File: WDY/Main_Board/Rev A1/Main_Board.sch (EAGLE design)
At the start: 188 parts, among them J1 22-05-7028-02, J10 22-05-7038-03, J11 22-05-7028-02, J12 22-05-7028-02, J13 22-05-7028-02, J14 22-05-7028-02, J15 22-05-7058-05, J2 22-05-7028-02, J3 22-05-7048-04, J4 22-05-7048-04, J5 1241050-5, J6 90814-0208, J7 90814-0206, J8 90814-0208, J9 22-05-7038-03, K1 G6K-2G-Y, K2 G6K-2G-Y, K3 G6K-2G-Y, K4 G6K-2G-Y, P1 RB1-125BAG1A, SW1 B3FS-1015, SW2 B3FS-1015, T1 MMBT2222AL, U1 LPC1768FBD100, U11 SN74LVC3G17DCTR, U2 SN74LVC3G17DCTR, U3 SN74LVC3G17DCTR, U4 TPL0401A, U5 AT24C512C-SSHM-B, U6 SN74LVC2G17DBVR, U7 SN74LVC2G17DBVR, U8 LT1767EMS8E-5PBF, U9 TC1264-3.3, X1 FC-135, X2 MSTBA2

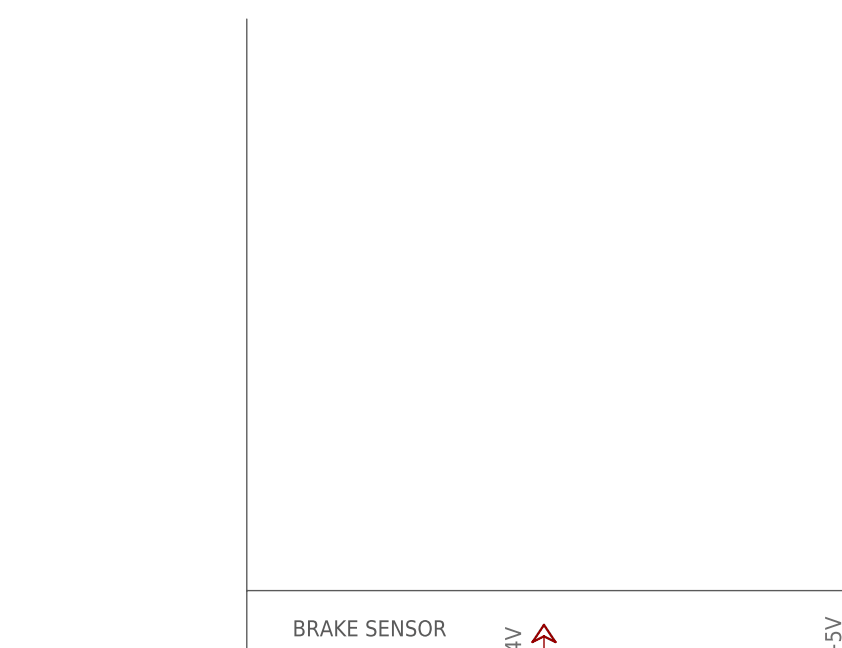
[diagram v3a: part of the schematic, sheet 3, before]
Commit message: Finishing routing and adding FTDI connector
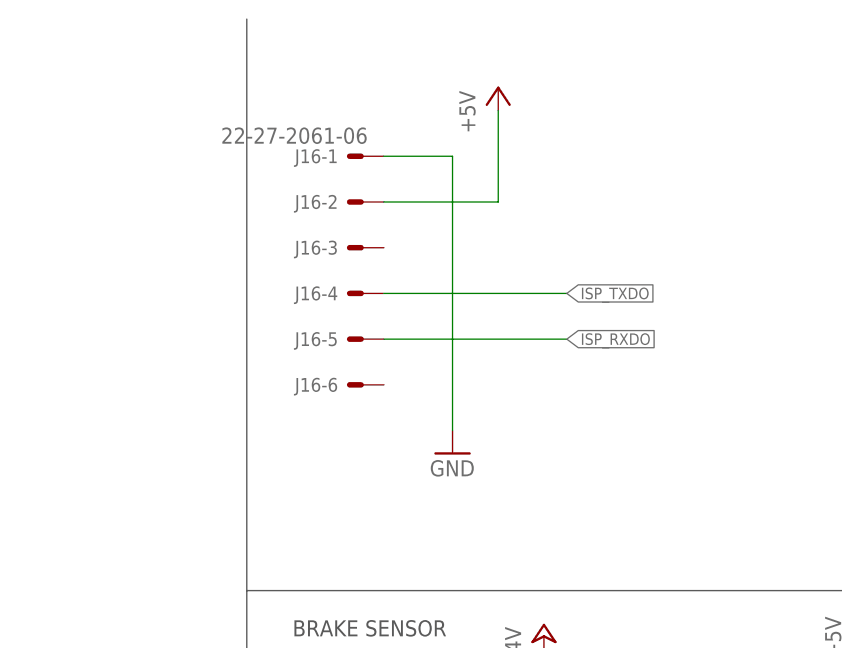
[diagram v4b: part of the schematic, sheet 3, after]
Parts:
- added J16: 22-27-2061-06, con-molex:22-27-2061-06
- added TP3: TPB1,27, testpad:TPB1,27
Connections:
- net +5V: now also J16-2.S
- net EEPROM_SCL: now also U1.P0[28]/SCL0/USB_SCL
- net EEPROM_SDA: now also U1.P0[27]/SDA0/USB_SDA
- net GND: now also J16-1.S, TP3.TP
- net HMI_LCD_BACKLIGHT: now also U1.P0[22]/RTS1/TD1
- net ISP_RXDO: now also J16-5.S
- net ISP_TXDO: now also J16-4.S
- net VBAT+: now also U1.VBAT
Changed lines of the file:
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@@
 <class number="1" name="signal" width="0.1778" drill="0.35">
 </class>
-<class number="2" name="supply" width="0.4064" drill="0.5">
+<class number="2" name="supply" width="0.007740625" drill="0.5">
 </class>
 </classes>
@@
 <part name="GND89" library="supply1" deviceset="GND" device=""/>
 <part name="R70" library="rcl" deviceset="R-EU_" device="R0603" value="100"/>
+<part name="J16" library="con-molex" deviceset="22-?-06" device="27-2061"/>
+<part name="P+23" library="supply1" deviceset="+5V" device=""/>
+<part name="GND90" library="supply1" deviceset="GND" device=""/>
+<part name="TP3" library="testpad" deviceset="TP" device="B1,27"/>
 </parts>
 <sheets>
@@
 </segment>
 <segment>
-<wire x1="132.08" y1="172.72" x2="124.46" y2="172.72" width="0.1524" layer="91"/>
 <label x="124.46" y="172.72" size="1.27" layer="95" rot="R180" xref="yes"/>
+<pinref part="U1" gate="A" pin="P0[27]/SDA0/USB_SDA"/>
+<wire x1="124.46" y1="172.72" x2="132.08" y2="172.72" width="0.1524" layer="91"/>
 </segment>
 </net>
@@
 </segment>
 <segment>
-<wire x1="132.08" y1="175.26" x2="124.46" y2="175.26" width="0.1524" layer="91"/>
 <label x="124.46" y="175.26" size="1.27" layer="95" rot="R180" xref="yes"/>
+<pinref part="U1" gate="A" pin="P0[28]/SCL0/USB_SCL"/>
+<wire x1="124.46" y1="175.26" x2="132.08" y2="175.26" width="0.1524" layer="91"/>
 </segment>
 </net>
@@
 </segment>
 <segment>
-<wire x1="134.62" y1="187.96" x2="124.46" y2="187.96" width="0.1524" layer="91"/>
 <label x="124.46" y="187.96" size="1.27" layer="95" rot="R180" xref="yes"/>
+<pinref part="U1" gate="A" pin="VBAT"/>
+<wire x1="124.46" y1="187.96" x2="132.08" y2="187.96" width="0.1524" layer="91"/>
+</segment>
+</net>
+<net name="HMI_LCD_BACKLIGHT" class="0">
+<segment>
+<wire x1="314.96" y1="121.92" x2="320.04" y2="121.92" width="0.1524" layer="91"/>
+<label x="320.04" y="121.92" size="1.27" layer="95" xref="yes"/>
+<pinref part="U1" gate="A" pin="P0[22]/RTS1/TD1"/>
 </segment>
 </net>
@@
 <instance part="U$12" gate="A" x="40.64" y="248.92"/>
 <instance part="U$13" gate="A" x="320.04" y="167.64"/>
+<instance part="J16" gate="-1" x="134.62" y="241.3" rot="MR0"/>
+<instance part="J16" gate="-2" x="134.62" y="236.22" rot="MR0"/>
+<instance part="J16" gate="-3" x="134.62" y="231.14" rot="MR0"/>
+<instance part="J16" gate="-4" x="134.62" y="226.06" rot="MR0"/>
+<instance part="J16" gate="-5" x="134.62" y="220.98" rot="MR0"/>
+<instance part="J16" gate="-6" x="134.62" y="215.9" rot="MR0"/>
+<instance part="P+23" gate="1" x="149.86" y="248.92"/>
+<instance part="GND90" gate="1" x="144.78" y="208.28"/>
 </instances>
 <busses>
@@
 <wire x1="320.04" y1="137.16" x2="320.04" y2="134.62" width="0.1524" layer="91"/>
 </segment>
+<segment>
+<pinref part="J16" gate="-1" pin="S"/>
+<pinref part="GND90" gate="1" pin="GND"/>
+<wire x1="137.16" y1="241.3" x2="144.78" y2="241.3" width="0.1524" layer="91"/>
+<wire x1="144.78" y1="241.3" x2="144.78" y2="210.82" width="0.1524" layer="91"/>
+</segment>
 </net>
 <net name="+3V3" class="2">
@@
 <junction x="25.4" y="86.36"/>
 </segment>
+<segment>
+<pinref part="J16" gate="-2" pin="S"/>
+<wire x1="137.16" y1="236.22" x2="149.86" y2="236.22" width="0.1524" layer="91"/>
+<wire x1="149.86" y1="236.22" x2="149.86" y2="246.38" width="0.1524" layer="91"/>
+<pinref part="P+23" gate="1" pin="+5V"/>
+</segment>
 </net>
 <net name="N$21" class="0">
@@
 </segment>
 </net>
+<net name="ISP_TXDO" class="1">
+<segment>
+<pinref part="J16" gate="-4" pin="S"/>
+<wire x1="137.16" y1="226.06" x2="157.48" y2="226.06" width="0.1524" layer="91"/>
+<label x="157.48" y="226.06" size="1.27" layer="95" xref="yes"/>
+</segment>
+</net>
+<net name="ISP_RXDO" class="1">
+<segment>
+<pinref part="J16" gate="-5" pin="S"/>
+<wire x1="137.16" y1="220.98" x2="157.48" y2="220.98" width="0.1524" layer="91"/>
+<label x="157.48" y="220.98" size="1.27" layer="95" xref="yes"/>
+</segment>
+</net>
 </nets>
 </sheet>
@@
 <instance part="MP3" gate="1" x="327.66" y="236.22"/>
 <instance part="MP4" gate="1" x="355.6" y="236.22"/>
+<instance part="TP3" gate="G$1" x="106.68" y="195.58" rot="R180"/>
 </instances>
 <busses>
@@
 <wire x1="106.68" y1="200.66" x2="88.9" y2="200.66" width="0.1524" layer="91"/>
 <junction x="88.9" y="200.66"/>
+<pinref part="TP3" gate="G$1" pin="TP"/>
+<wire x1="106.68" y1="198.12" x2="106.68" y2="200.66" width="0.1524" layer="91"/>
+<junction x="106.68" y="200.66"/>
 </segment>
 <segment>

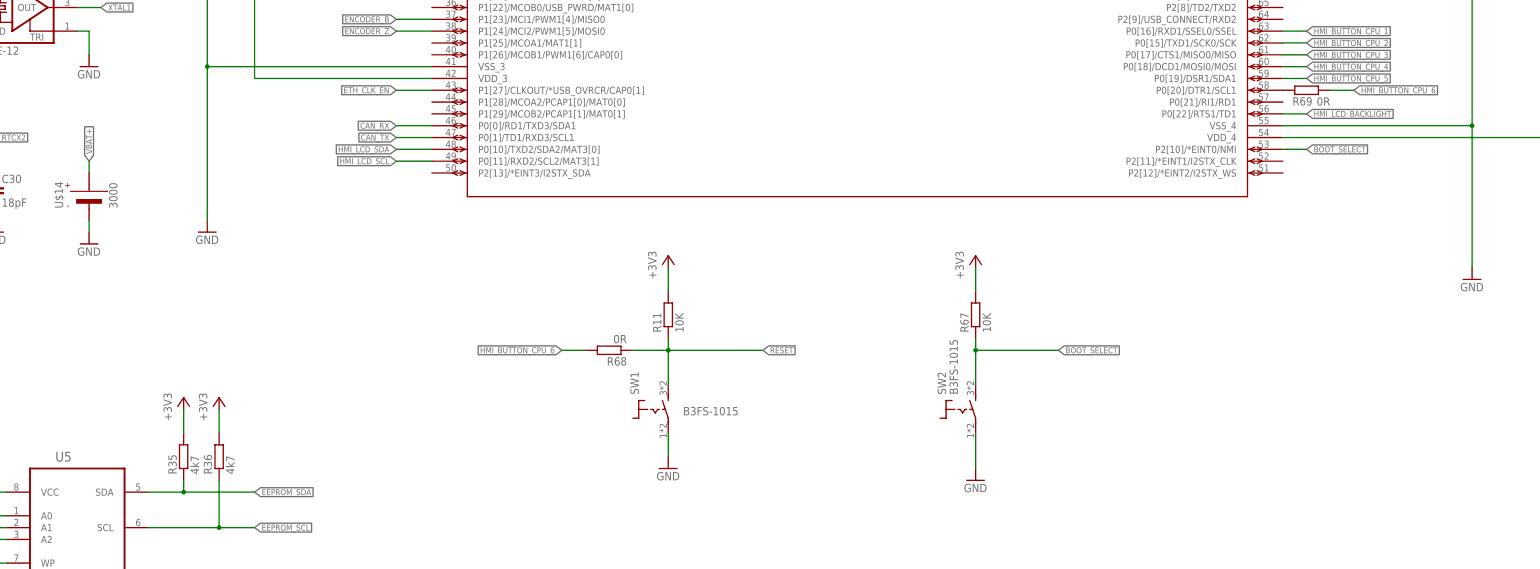
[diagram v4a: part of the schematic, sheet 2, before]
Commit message: Fix :  HMI_BUTTON_CPU_6 configuration is misleading
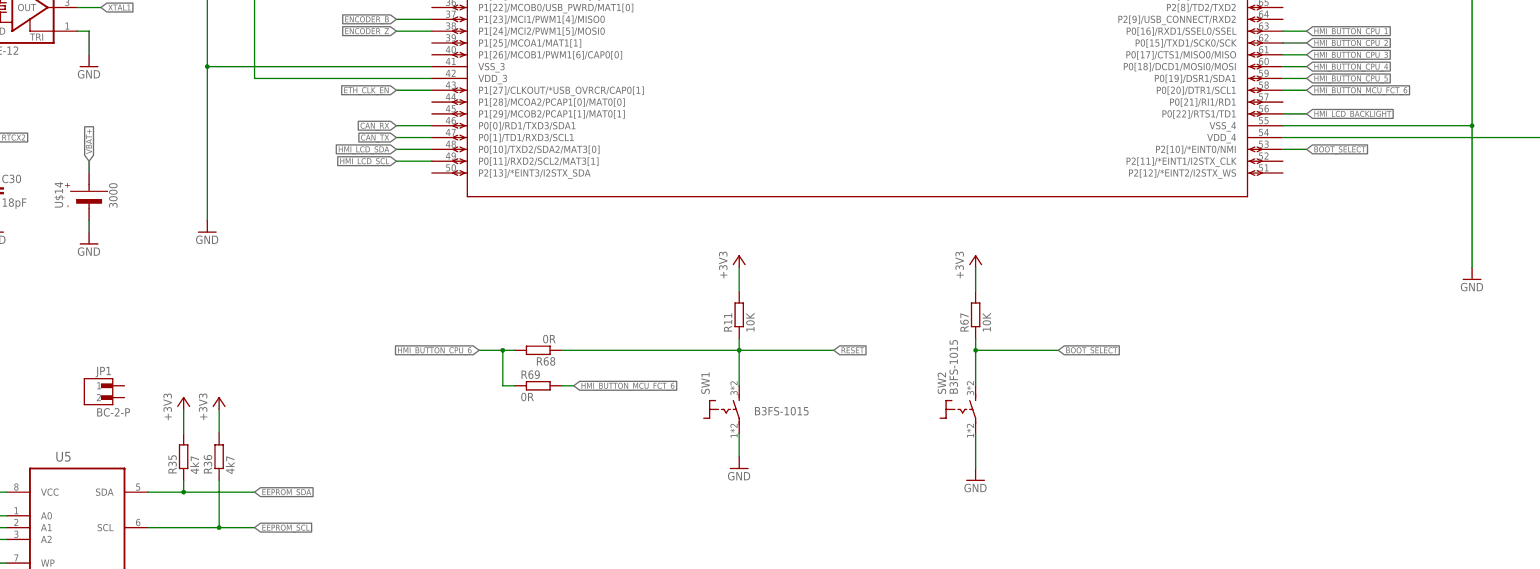
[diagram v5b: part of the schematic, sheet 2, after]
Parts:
- added JP1: BC-2-P, exmachina:BC-2-P
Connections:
- net N$5 renamed HMI_BUTTON_MCU_FCT_6
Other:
- moved on the sheet: R11, R68, R69, SW1
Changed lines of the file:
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@@
 <part name="GND90" library="supply1" deviceset="GND" device=""/>
 <part name="TP3" library="testpad" deviceset="TP" device="B1,27"/>
+<part name="JP1" library="exmachina" deviceset="BC-2-?" device="P"/>
 </parts>
 <sheets>
@@
 <instance part="GND85" gate="1" x="10.16" y="132.08"/>
 <instance part="+3V43" gate="G$1" x="10.16" y="157.48"/>
-<instance part="SW1" gate="G$1" x="180.34" y="58.42" smashed="yes">
-<attribute name="NAME" x="176.53" y="61.595" size="1.778" layer="95" rot="R90"/>
-<attribute name="VALUE" x="186.055" y="57.15" size="1.778" layer="96"/>
+<instance part="SW1" gate="G$1" x="195.58" y="58.42" smashed="yes">
+<attribute name="NAME" x="191.77" y="61.595" size="1.778" layer="95" rot="R90"/>
+<attribute name="VALUE" x="201.295" y="57.15" size="1.778" layer="96"/>
 </instance>
 <instance part="SW2" gate="G$1" x="246.38" y="58.42"/>
-<instance part="R11" gate="G$1" x="182.88" y="78.74" rot="R90"/>
+<instance part="R11" gate="G$1" x="198.12" y="78.74" rot="R90"/>
 <instance part="R67" gate="G$1" x="248.92" y="78.74" rot="R90"/>
-<instance part="+3V12" gate="G$1" x="182.88" y="91.44"/>
+<instance part="+3V12" gate="G$1" x="198.12" y="91.44"/>
 <instance part="+3V13" gate="G$1" x="248.92" y="91.44"/>
-<instance part="GND86" gate="1" x="182.88" y="45.72"/>
+<instance part="GND86" gate="1" x="198.12" y="45.72"/>
 <instance part="GND87" gate="1" x="248.92" y="43.18"/>
-<instance part="R68" gate="G$1" x="170.18" y="71.12" rot="R180"/>
-<instance part="R69" gate="G$1" x="320.04" y="127" smashed="yes" rot="R180">
-<attribute name="NAME" x="321.31" y="125.5014" size="1.778" layer="95" rot="R180"/>
-<attribute name="VALUE" x="325.12" y="125.476" size="1.778" layer="96" rot="R180"/>
-</instance>
+<instance part="R68" gate="G$1" x="154.94" y="71.12" rot="R180"/>
+<instance part="R69" gate="G$1" x="154.94" y="63.5"/>
 <instance part="U$14" gate="A" x="58.42" y="104.14" rot="R90"/>
 <instance part="GND89" gate="1" x="58.42" y="93.98"/>
+<instance part="JP1" gate="G$1" x="60.96" y="63.5"/>
 </instances>
 <busses>
@@
 <pinref part="+3V12" gate="G$1" pin="+3V3"/>
 <pinref part="R11" gate="G$1" pin="2"/>
-<wire x1="182.88" y1="88.9" x2="182.88" y2="83.82" width="0.1524" layer="91"/>
+<wire x1="198.12" y1="88.9" x2="198.12" y2="83.82" width="0.1524" layer="91"/>
 </segment>
 <segment>
@@
 <pinref part="GND86" gate="1" pin="GND"/>
 <pinref part="SW1" gate="G$1" pin="2"/>
-<wire x1="182.88" y1="48.26" x2="182.88" y2="53.34" width="0.1524" layer="91"/>
+<wire x1="198.12" y1="48.26" x2="198.12" y2="53.34" width="0.1524" layer="91"/>
 </segment>
 <segment>
@@
 <net name="HMI_BUTTON_CPU_6" class="0">
 <segment>
-<label x="330.2" y="127" size="1.27" layer="95" xref="yes"/>
+<pinref part="R68" gate="G$1" pin="2"/>
+<wire x1="149.86" y1="71.12" x2="147.32" y2="71.12" width="0.1524" layer="91"/>
+<label x="142.24" y="71.12" size="1.27" layer="95" rot="R180" xref="yes"/>
+<wire x1="147.32" y1="71.12" x2="142.24" y2="71.12" width="0.1524" layer="91"/>
+<wire x1="149.86" y1="63.5" x2="147.32" y2="63.5" width="0.1524" layer="91"/>
+<wire x1="147.32" y1="63.5" x2="147.32" y2="71.12" width="0.1524" layer="91"/>
+<junction x="147.32" y="71.12"/>
 <pinref part="R69" gate="G$1" pin="1"/>
-<wire x1="325.12" y1="127" x2="330.2" y2="127" width="0.1524" layer="91"/>
-</segment>
-<segment>
-<pinref part="R68" gate="G$1" pin="2"/>
-<wire x1="165.1" y1="71.12" x2="160.02" y2="71.12" width="0.1524" layer="91"/>
-<label x="160.02" y="71.12" size="1.27" layer="95" rot="R180" xref="yes"/>
 </segment>
 </net>
@@
 <pinref part="SW1" gate="G$1" pin="1"/>
 <pinref part="R11" gate="G$1" pin="1"/>
-<wire x1="182.88" y1="63.5" x2="182.88" y2="71.12" width="0.1524" layer="91"/>
-<wire x1="182.88" y1="71.12" x2="182.88" y2="73.66" width="0.1524" layer="91"/>
-<wire x1="182.88" y1="71.12" x2="203.2" y2="71.12" width="0.1524" layer="91"/>
-<junction x="182.88" y="71.12"/>
-<label x="203.2" y="71.12" size="1.27" layer="95" xref="yes"/>
+<wire x1="198.12" y1="63.5" x2="198.12" y2="71.12" width="0.1524" layer="91"/>
+<wire x1="198.12" y1="71.12" x2="198.12" y2="73.66" width="0.1524" layer="91"/>
+<wire x1="198.12" y1="71.12" x2="218.44" y2="71.12" width="0.1524" layer="91"/>
+<junction x="198.12" y="71.12"/>
+<label x="218.44" y="71.12" size="1.27" layer="95" xref="yes"/>
 <pinref part="R68" gate="G$1" pin="1"/>
-<wire x1="175.26" y1="71.12" x2="182.88" y2="71.12" width="0.1524" layer="91"/>
+<wire x1="198.12" y1="71.12" x2="160.02" y2="71.12" width="0.1524" layer="91"/>
 </segment>
 <segment>
@@
 </segment>
 </net>
-<net name="N$5" class="0">
-<segment>
-<pinref part="R69" gate="G$1" pin="2"/>
-<pinref part="U1" gate="A" pin="P0[20]/DTR1/SCL1"/>
-</segment>
-</net>
 <net name="VBAT+" class="0">
 <segment>
@@
 </segment>
 </net>
+<net name="HMI_BUTTON_MCU_FCT_6" class="0">
+<segment>
+<pinref part="U1" gate="A" pin="P0[20]/DTR1/SCL1"/>
+<wire x1="314.96" y1="127" x2="320.04" y2="127" width="0.1524" layer="91"/>
+<label x="320.04" y="127" size="1.27" layer="95" xref="yes"/>
+</segment>
+<segment>
+<pinref part="R69" gate="G$1" pin="2"/>
+<wire x1="160.02" y1="63.5" x2="162.56" y2="63.5" width="0.1524" layer="91"/>
+<label x="162.56" y="63.5" size="1.27" layer="95" xref="yes"/>
+</segment>
+</net>
